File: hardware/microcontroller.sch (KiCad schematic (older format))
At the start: 19 parts, among them P201 CONN_02X03, SW201 SPST, SW202 SPST, U201 LPC11C14

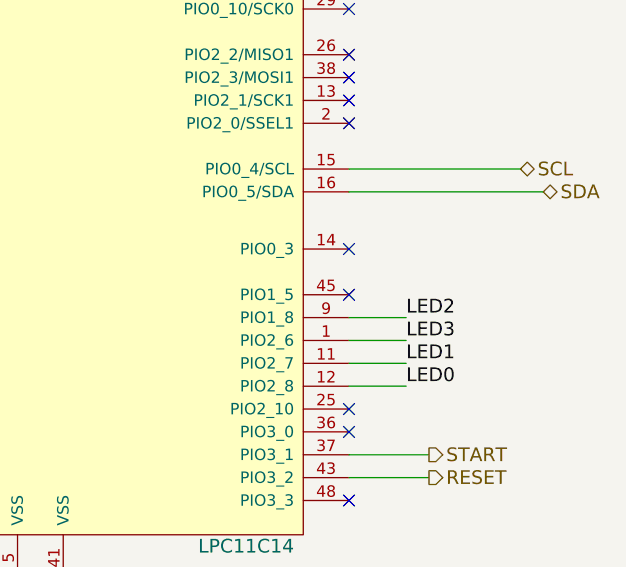
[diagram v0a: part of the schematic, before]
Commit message: Updated pcb layout
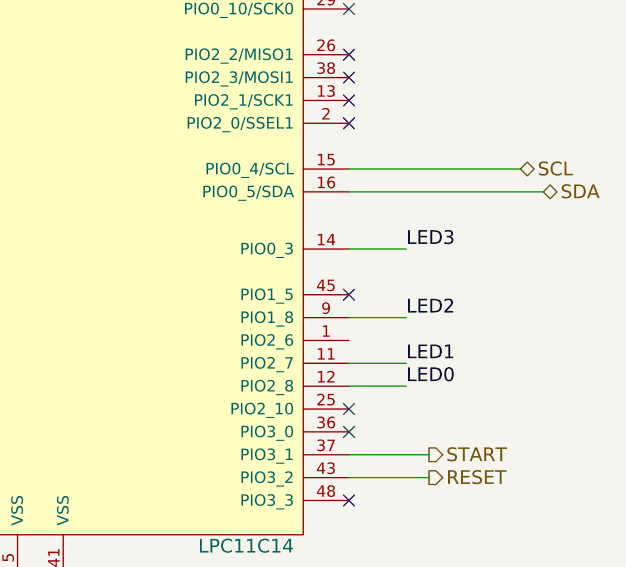
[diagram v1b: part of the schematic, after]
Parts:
- P201: footprint Connectors_Molex:Connector_Microfit3_Header_02x03_Angled_43045-060x -> Connectors_Molex:Molex_Microfit3_Header_02x03_Angled_43045-060x
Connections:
- net LED3: now also U201.14 (PIO0_3); no longer U201.1 (PIO2_6)
- no-connect marks 26 -> 25
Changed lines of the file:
@@
 $EndComp
 $Comp
-L GND #PWR01
+L GND #PWR02
 U 1 1 57AA1B4A
 P 8150 5800
-F 0 "#PWR01" H 8150 5550 50  0001 C CNN
+F 0 "#PWR02" H 8150 5550 50  0001 C CNN
 F 1 "GND" H 8150 5650 50  0000 C CNN
 F 2 "" H 8150 5800 50  0000 C CNN
@@
 $EndComp
 $Comp
-L GND #PWR02
+L GND #PWR03
 U 1 1 57AA1B71
 P 6000 3550
-F 0 "#PWR02" H 6000 3300 50  0001 C CNN
+F 0 "#PWR03" H 6000 3300 50  0001 C CNN
 F 1 "GND" H 6000 3400 50  0000 C CNN
 F 2 "" H 6000 3550 50  0000 C CNN
@@
 $EndComp
 $Comp
-L GND #PWR03
+L GND #PWR04
 U 1 1 57AA1BB4
 P 8800 1450
-F 0 "#PWR03" H 8800 1200 50  0001 C CNN
+F 0 "#PWR04" H 8800 1200 50  0001 C CNN
 F 1 "GND" H 8800 1300 50  0000 C CNN
 F 2 "" H 8800 1450 50  0000 C CNN
@@
 NoConn ~ 9500 3450
 NoConn ~ 9500 3550
-NoConn ~ 9500 4100
 NoConn ~ 6850 5200
 NoConn ~ 6850 3900
@@
 ALERT
 $Comp
-L +3.3V #PWR04
+L +3.3V #PWR05
 U 1 1 57AA2167
 P 5650 1100
-F 0 "#PWR04" H 5650 950 50  0001 C CNN
+F 0 "#PWR05" H 5650 950 50  0001 C CNN
 F 1 "+3.3V" H 5650 1240 50  0000 C CNN
 F 2 "" H 5650 1100 50  0000 C CNN
@@
 $EndComp
 $Comp
-L GND #PWR05
+L GND #PWR06
 U 1 1 57AA2ED7
 P 4750 3000
-F 0 "#PWR05" H 4750 2750 50  0001 C CNN
+F 0 "#PWR06" H 4750 2750 50  0001 C CNN
 F 1 "GND" H 4750 2850 50  0000 C CNN
 F 2 "" H 4750 3000 50  0000 C CNN
@@
 $EndComp
 $Comp
-L GND #PWR06
+L GND #PWR07
 U 1 1 57AA3511
 P 3750 1800
-F 0 "#PWR06" H 3750 1550 50  0001 C CNN
+F 0 "#PWR07" H 3750 1550 50  0001 C CNN
 F 1 "GND" H 3750 1650 50  0000 C CNN
 F 2 "" H 3750 1800 50  0000 C CNN
@@
 NoConn ~ 6850 3400
 $Comp
-L +5V #PWR07
+L +5V #PWR08
 U 1 1 57DEE2BD
 P 2400 1800
-F 0 "#PWR07" H 2400 1650 50  0001 C CNN
+F 0 "#PWR08" H 2400 1650 50  0001 C CNN
 F 1 "+5V" H 2400 1940 50  0000 C CNN
 F 2 "" H 2400 1800 60  0000 C CNN
@@
 F 0 "P201" H 3300 2250 50  0000 C CNN
 F 1 "CONN_02X03" H 3300 1850 50  0000 C CNN
-F 2 "Connectors_Molex:Connector_Microfit3_Header_02x03_Angled_43045-060x" H 3300 850 60  0001 C CNN
+F 2 "Connectors_Molex:Molex_Microfit3_Header_02x03_Angled_43045-060x" H 3300 850 60  0001 C CNN
 F 3 "" H 3300 850 60  0000 C CNN
 	1    3300 2050
@@
 Text Label 9750 4400 0    60   ~ 0
 LED2
-Text Label 9750 4500 0    60   ~ 0
+Text Label 9750 4100 0    60   ~ 0
 LED3
 Text Label 9750 4600 0    60   ~ 0
@@
 NoConn ~ 9500 5200
 $Comp
-L GND #PWR08
+L GND #PWR09
 U 1 1 57E6C976
 P 3350 5650
-F 0 "#PWR08" H 3350 5400 50  0001 C CNN
+F 0 "#PWR09" H 3350 5400 50  0001 C CNN
 F 1 "GND" H 3350 5500 50  0000 C CNN
 F 2 "" H 3350 5650 60  0000 C CNN
@@
 $EndComp
 $Comp
-L GND #PWR09
+L GND #PWR010
 U 1 1 57E789B8
 P 7200 750
-F 0 "#PWR09" H 7200 500 50  0001 C CNN
+F 0 "#PWR010" H 7200 500 50  0001 C CNN
 F 1 "GND" H 7200 600 50  0000 C CNN
 F 2 "" H 7200 750 60  0000 C CNN
@@
 	9500 4600 9750 4600
 Wire Wire Line
-	9500 4500 9750 4500
-Wire Wire Line
 	9500 4400 9750 4400
-Wire Wire Line
-	9500 4700 9750 4700
-Wire Wire Line
-	2800 1950 3050 1950
-Wire Wire Line
-	2400 1800 2400 2050
-Wire Wire Line
-	2400 2050 3050 2050
 Wire Wire Line
 	2800 2150 3050 2150
@@
 Wire Wire Line
 	7450 750  7200 750
+Wire Wire Line
+	2800 1950 3050 1950
+Wire Wire Line
+	2400 2050 3050 2050
+Wire Wire Line
+	2400 1800 2400 2050
+Wire Wire Line
+	9500 4700 9750 4700
+Wire Wire Line
+	9500 4100 9750 4100
 $EndSCHEMATC
